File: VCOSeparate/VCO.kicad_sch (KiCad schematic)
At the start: 47 parts, among them IC1 V3340M, U1 Opamp_Dual

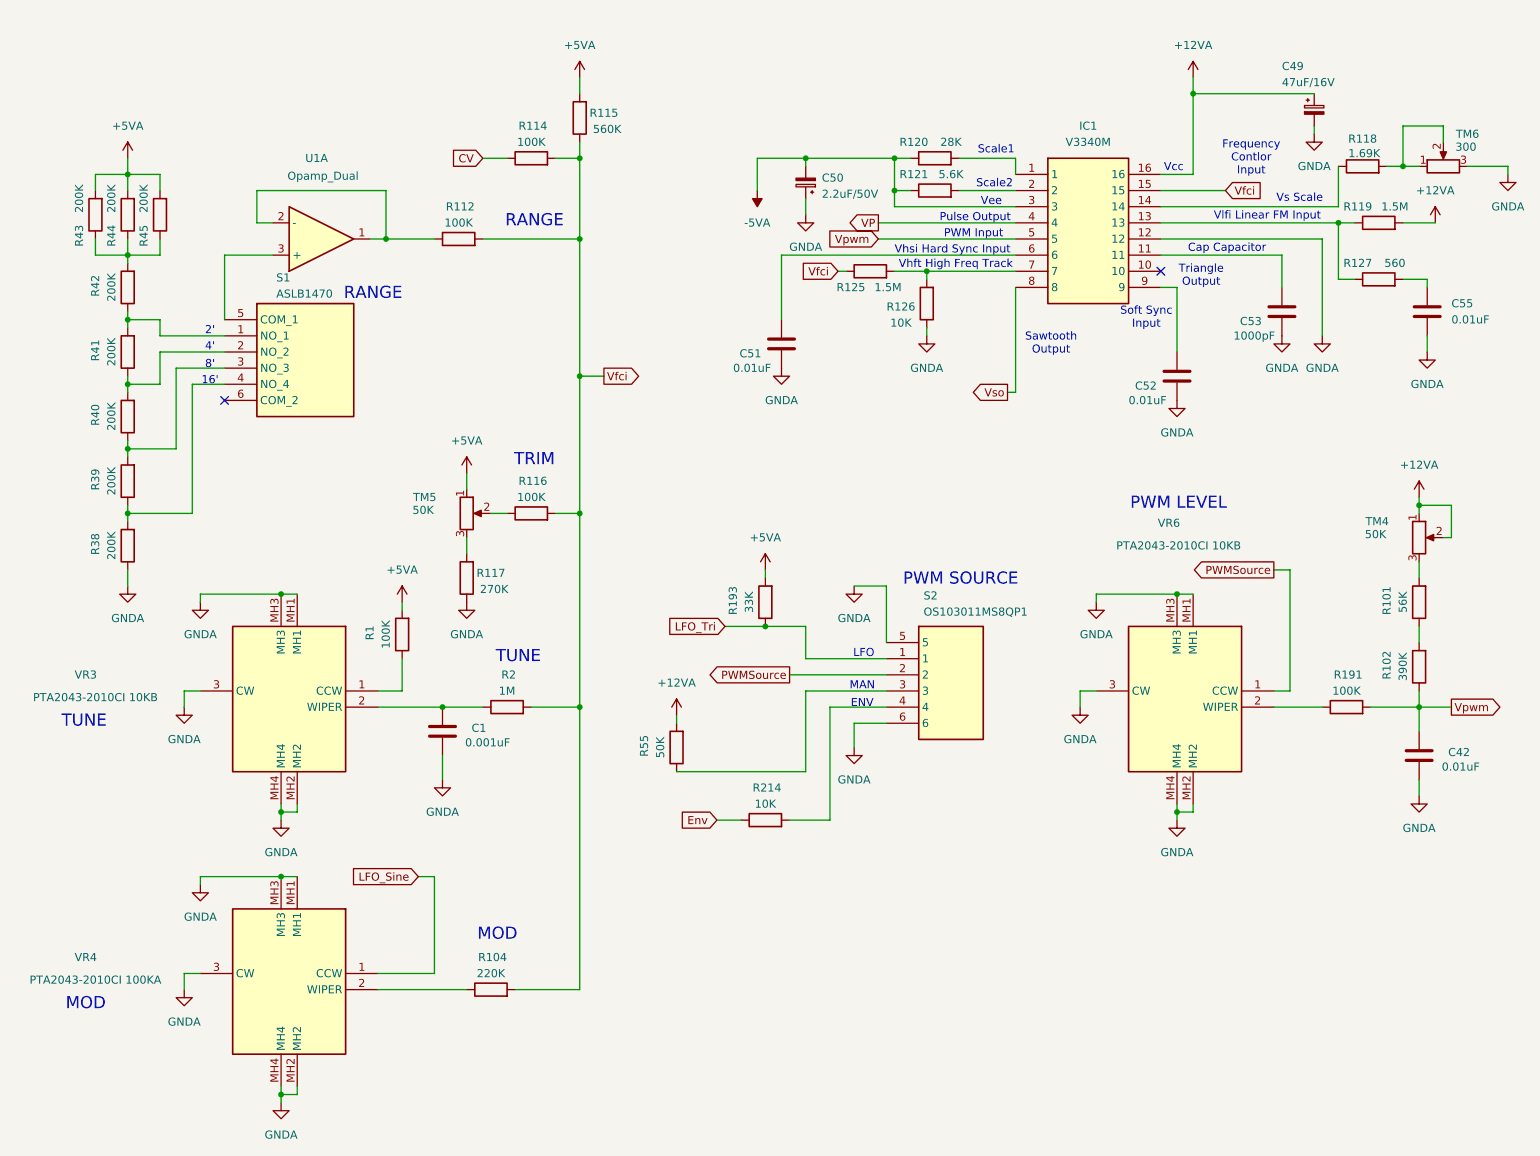
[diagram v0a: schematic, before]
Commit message: MC2
アクセントレベルを追加したEGACCを登録
回路全般部品配置済
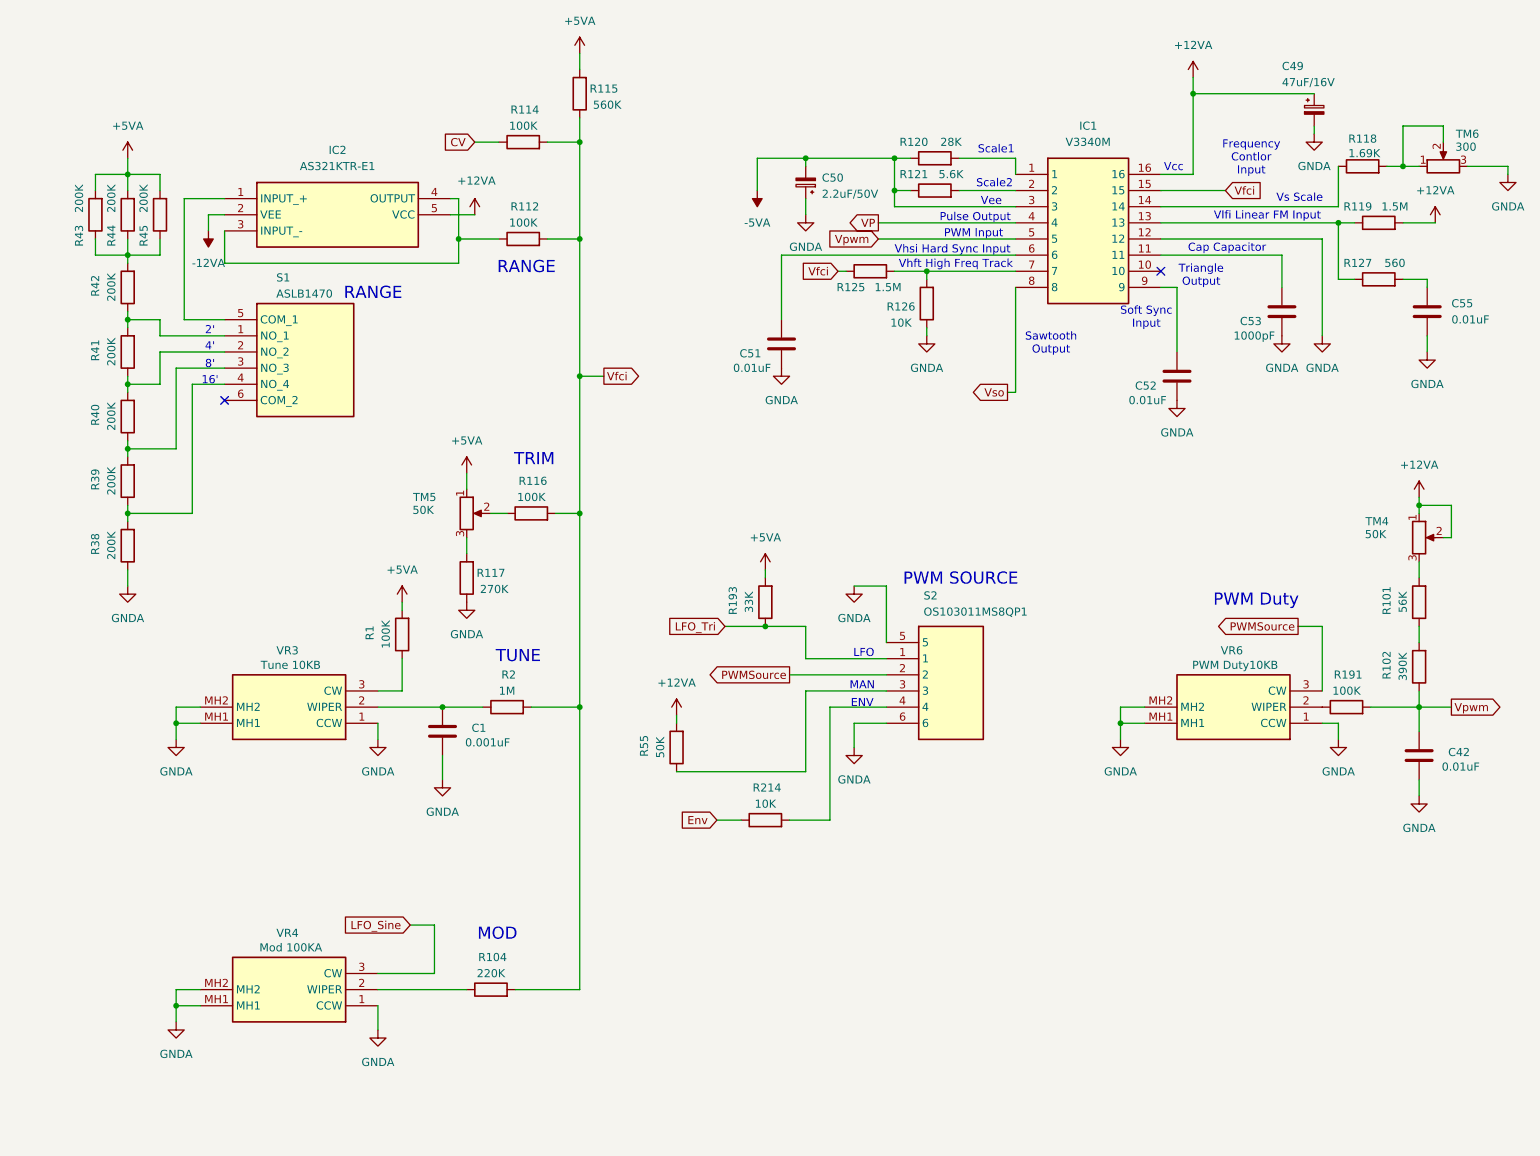
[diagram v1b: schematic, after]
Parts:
- removed U1: Opamp_Dual, Package_DIP:DIP-8_W7.62mm_LongPads, symbol Device:Opamp_Dual
- removed VR3, VR6: PTA2043-2010CI 10KB, PTA20432010CIB104, symbol SamacSys_Parts:PTA2043-2010CIB104
- removed VR4: PTA2043-2010CI 100KA, PTA20432010CIB104, symbol SamacSys_Parts:PTA2043-2010CIB104
- added IC2: AS321KTR-E1, SOT95P282X145-5N, symbol SamacSys_Parts:AS321KTR-E1
- added VR3: Tune 10KB, SamacSys_Parts:RK09D117000B, symbol SamacSys_Parts:RK09D117000B
- added VR4: Mod 100KA, SamacSys_Parts:RK09D117000B, symbol SamacSys_Parts:RK09D117000B
- added VR6: PWM Duty10KB, SamacSys_Parts:RK09D117000B, symbol SamacSys_Parts:RK09D117000B
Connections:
- net +12VA: now also IC2.5 (VCC)
- net GNDA: now also VR3.1 (CCW), VR3.MH1, VR3.MH2, VR4.1 (CCW), VR4.MH1, VR4.MH2, VR6.1 (CCW), VR6.MH1, VR6.MH2
- net LFO_Sine: now also VR4.3 (CW)
- net PWMSource: now also VR6.3 (CW)
- net at R112.1: now also IC2.3 (INPUT_-), IC2.4 (OUTPUT)
- net at S1.5 (COM_1): now also IC2.1 (INPUT_+)
- net at R104.1: now also VR4.2 (WIPER)
- net at R1.1: now also VR3.3 (CW)
- net at C1.2, R2.1: now also VR3.2 (WIPER)
- net at R191.1: now also VR6.2 (WIPER)
- new net -12VA: IC2.2 (VEE)
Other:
- note added: "PWM Duty"
- note removed: "PWM LEVEL"
- moved on the sheet: R112, R114, R115
